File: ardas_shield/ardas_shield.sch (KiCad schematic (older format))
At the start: 36 parts, among them CON1 SD_Card, IC1 DS1307, P1 CONN_10, P10 CONN_01X03, P2 CONN_8, P3 CONN_8, P4 CONN_ICSP, P5 CONN_6, P6 TTL_COMM, P7 CONN_01X03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

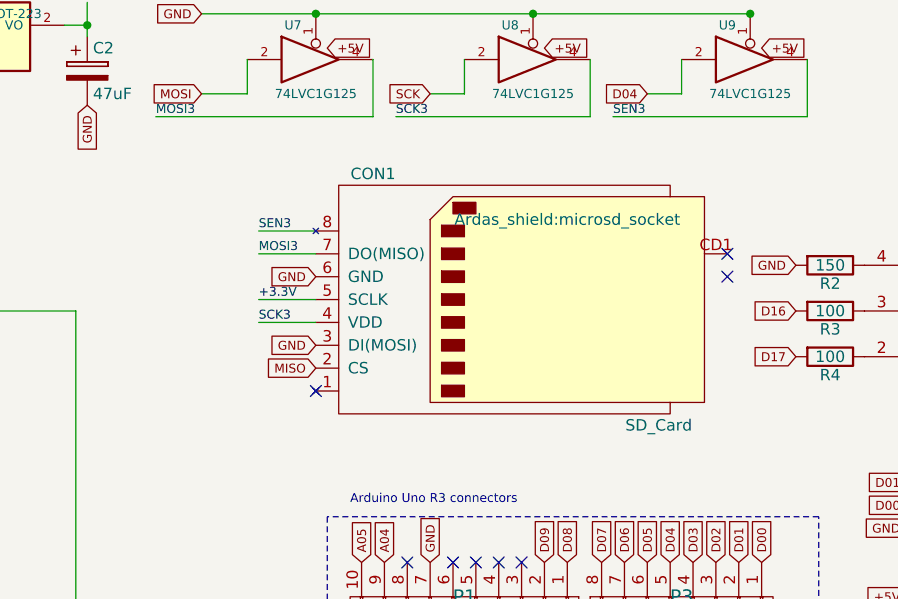
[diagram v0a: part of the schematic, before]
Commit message: changed resitances arrays footprints
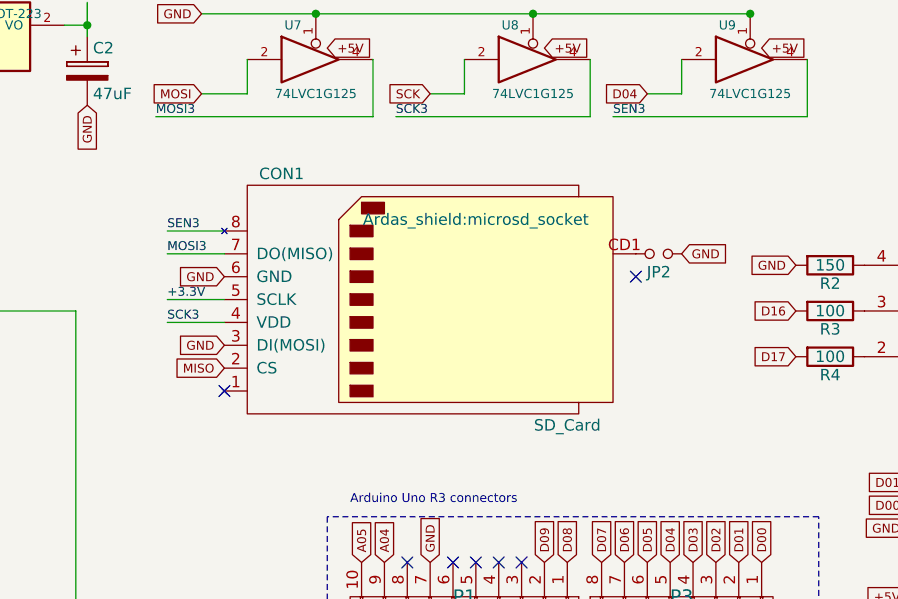
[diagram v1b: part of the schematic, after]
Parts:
- added JP2: Jumper_NO_Small, RTC_Ardas_test:small_no_jumper, symbol Jumper_NO_Small
- RP1, RP2, RP3, RP4, RP5: footprint Ardas_shield:R_Array_Convex_4x1206 -> kicad-gfa local:R_Array_Convex_4x0603
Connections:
- net GND: now also JP2.1
- net at CON1.CD1: now also JP2.2
- no-connect marks 22 -> 21
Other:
- moved on the sheet: CON1
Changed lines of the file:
@@
 $EndDescr
 $Comp
-L PWR_FLAG #FLG01
+L PWR_FLAG #FLG2
 U 1 1 55782956
 P 800 1100
-F 0 "#FLG01" H 800 1195 30  0001 C CNN
+F 0 "#FLG2" H 800 1195 30  0001 C CNN
 F 1 "PWR_FLAG" H 800 1280 30  0000 C CNN
 F 2 "" H 800 1100 60  0000 C CNN
@@
 NoConn ~ 4300 6600
 $Comp
-L +5V #PWR02
+L +5V #PWR1
 U 1 1 56548203
 P 1000 700
-F 0 "#PWR02" H 1000 790 20  0001 C CNN
+F 0 "#PWR1" H 1000 790 20  0001 C CNN
 F 1 "+5V" H 1000 790 30  0000 C CNN
 F 2 "" H 1000 700 60  0000 C CNN
@@
 D14
 $Comp
-L PWR_FLAG #FLG03
+L PWR_FLAG #FLG1
 U 1 1 55782922
 P 800 700
-F 0 "#FLG03" H 800 795 30  0001 C CNN
+F 0 "#FLG1" H 800 795 30  0001 C CNN
 F 1 "PWR_FLAG" H 800 880 30  0000 C CNN
 F 2 "" H 800 700 60  0000 C CNN
@@
 Text GLabel 10600 1250 0    39   Input ~ 0
 SCK
-Text GLabel 10100 2350 0    39   Input ~ 0
-GND
-Text GLabel 10100 2450 0    39   Input ~ 0
+Text GLabel 9700 2350 0    39   Input ~ 0
+GND
+Text GLabel 9700 2450 0    39   Input ~ 0
 MISO
-Text GLabel 10100 2050 0    39   Input ~ 0
-GND
-Text Label 9850 2250 0    39   ~ 0
+Text GLabel 9700 2050 0    39   Input ~ 0
+GND
+Text Label 9450 2250 0    39   ~ 0
 SCK3
-Text Label 9850 2150 0    39   ~ 0
+Text Label 9450 2150 0    39   ~ 0
 +3.3V
 Text GLabel 8600 1250 3    39   Input ~ 0
 GND
-Text Label 9850 1950 0    39   ~ 0
+Text Label 9450 1950 0    39   ~ 0
 MOSI3
-Text Label 9850 1850 0    39   ~ 0
+Text Label 9450 1850 0    39   ~ 0
 SEN3
 $Comp
@@
 Text GLabel 12050 4150 2    39   Input ~ 0
 GND
-NoConn ~ 10100 2550
+NoConn ~ 9700 2550
 Text Notes 12850 3050 0    39   ~ 0
 Rx
@@
 F 0 "RP1" H 2450 2850 50  0000 C CNN
 F 1 "R_4x4.7k" H 2450 2350 50  0000 C CNN
-F 2 "Ardas_shield:R_Array_Convex_4x1206" H 2450 2400 60  0001 C CNN
+F 2 "kicad-gfa local:R_Array_Convex_4x0603" H 2450 2400 60  0001 C CNN
 F 3 "" H 2450 2400 60  0000 C CNN
 	1    2450 2400
@@
 F 0 "RP4" H 6750 5900 50  0000 C CNN
 F 1 "R_4x10k" H 6750 5400 50  0000 C CNN
-F 2 "Ardas_shield:R_Array_Convex_4x1206" H 6750 5450 60  0001 C CNN
+F 2 "kicad-gfa local:R_Array_Convex_4x0603" H 6750 5450 60  0001 C CNN
 F 3 "https://github.com/UMONS-GFA/kicad-gfa.pretty/blob/master/datasheets/1730408.pdf" H 6750 5450 60  0001 C CNN
 	1    6750 5450
@@
 F 0 "RP3" H 6750 4400 50  0000 C CNN
 F 1 "R_4x10k" H 6750 3900 50  0000 C CNN
-F 2 "Ardas_shield:R_Array_Convex_4x1206" H 6750 3950 60  0001 C CNN
+F 2 "kicad-gfa local:R_Array_Convex_4x0603" H 6750 3950 60  0001 C CNN
 F 3 "https://github.com/UMONS-GFA/kicad-gfa.pretty/blob/master/datasheets/1730408.pdf" H 6750 3950 60  0001 C CNN
 	1    6750 3950
@@
 NoConn ~ 11550 4150
 $Comp
-L GND #PWR04
+L GND #PWR2
 U 1 1 56583A97
 P 1000 1200
-F 0 "#PWR04" H 1000 1200 30  0001 C CNN
+F 0 "#PWR2" H 1000 1200 30  0001 C CNN
 F 1 "GND" H 1000 1130 30  0001 C CNN
 F 2 "" H 1000 1200 60  0000 C CNN
@@
 F 0 "RP2" H 4450 3550 50  0000 C CNN
 F 1 "R_4x10k" H 4450 3050 50  0000 C CNN
-F 2 "Ardas_shield:R_Array_Convex_4x1206" H 4450 3100 60  0001 C CNN
+F 2 "kicad-gfa local:R_Array_Convex_4x0603" H 4450 3100 60  0001 C CNN
 F 3 "" H 4450 3100 60  0000 C CNN
 	1    4450 3100
@@
 F 0 "RP5" H 7450 3550 50  0000 C CNN
 F 1 "R_4x10k" H 7450 3050 50  0000 C CNN
-F 2 "Ardas_shield:R_Array_Convex_4x1206" H 7450 3100 60  0001 C CNN
+F 2 "kicad-gfa local:R_Array_Convex_4x0603" H 7450 3100 60  0001 C CNN
 F 3 "https://github.com/UMONS-GFA/kicad-gfa.pretty/blob/master/datasheets/1730408.pdf" H 7450 3100 60  0001 C CNN
 	1    7450 3100
@@
 NoConn ~ 4600 2100
 NoConn ~ 2000 4200
-NoConn ~ 11900 1950
-NoConn ~ 11900 2050
+NoConn ~ 11500 2050
 NoConn ~ 13200 1000
 $Comp
 L SD_Card CON1
 U 1 1 5655FE06
-P 11000 2150
-F 0 "CON1" H 10350 2700 50  0000 C CNN
-F 1 "SD_Card" H 11600 1600 50  0000 C CNN
-F 2 "Ardas_shield:microsd_socket" H 11200 2500 50  0000 C CNN
-F 3 "" H 11000 2150 60  0000 C CNN
-	1    11000 2150
+P 10600 2150
+F 0 "CON1" H 9950 2700 50  0000 C CNN
+F 1 "SD_Card" H 11200 1600 50  0000 C CNN
+F 2 "Ardas_shield:microsd_socket" H 10800 2500 50  0000 C CNN
+F 3 "" H 10600 2150 60  0000 C CNN
+	1    10600 2150
 	1    0    0    -1
 $EndComp
@@
 	12300 5000 12300 3100
 Wire Wire Line
-	10100 1850 9850 1850
-Wire Wire Line
-	10100 1950 9850 1950
-Wire Wire Line
-	10100 2150 9850 2150
-Wire Wire Line
-	10100 2250 9850 2250
+	9700 1850 9450 1850
+Wire Wire Line
+	9700 1950 9450 1950
+Wire Wire Line
+	9700 2150 9450 2150
+Wire Wire Line
+	9700 2250 9450 2250
 Wire Wire Line
 	11700 1250 11550 1250
@@
 NoConn ~ 11950 4800
 NoConn ~ 12050 4800
+$Comp
+L Jumper_NO_Small JP2
+U 1 1 569E9D5A
+P 11600 1950
+F 0 "JP2" H 11600 2030 50  0000 C CNN
+F 1 "Jumper_NO_Small" H 11610 1890 50  0001 C CNN
+F 2 "RTC_Ardas_test:small_no_jumper" H 11600 1950 50  0001 C CNN
+F 3 "" H 11600 1950 50  0000 C CNN
+	1    11600 1950
+	-1   0    0    1
+$EndComp
+Text GLabel 11700 1950 2    39   Input ~ 0
+GND
 $EndSCHEMATC

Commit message: add details for BOM
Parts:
- BT1: MFN (none) -> KEYSTONE; MFP (none) -> 3000; Order_Code (none) -> 1650692
- CON1: MFN (none) -> MOLEX; MFP (none) -> 503182-1853; Order_Code (none) -> 2334075
- IC1: MFN (none) -> MAXIM INTEGRATED PRODUCTS; MFP (none) -> DS1307ZN+; Order_Code (none) -> 9725253
- P1: Contact_Termination_Type (none) -> Through Hole; MFN (none) -> FCI; MFP (none) -> 69190-410HLF; Order_Code (none) -> 1278412; Pitch_Spacing (none) -> 2.54mm
- P3: Contact_Termination _Type (none) -> Through Hole; MFN (none) -> FCI; MFP (none) -> 68000-208HLF; Order_Code (none) -> 1924194; Pitch_Spacing (none) -> 2.54mm
- P4: Contact_Termination_Type (none) -> Through Hole; Gender (none) -> Receptacle; MFN (none) -> TE CONNECTIVITY / AMP; MFP (none) -> 5-534206-3; Order_Code (none) -> 1266033; Pitch_Spacing (none) -> 2.54mm
- P5:  Pitch_Spacing (none) -> 2.54mm; Contact_Termination_Type (none) -> Through Hole; MFN (none) -> MOLEX; MFP (none) -> 22-28-4064; Order_Code (none) -> 2132359
- P6: Contact_Termination_Type (none) -> Through Hole; Gender (none) -> Header; MFN (none) -> MULTICOMP; MFP (none) -> MC34747; Order_Code (none) -> 1593427; Pitch_Spacing (none) -> 2.54mm
- R2: Case_Style (none) -> 0805 [2012 Metric]; MFN (none) -> YAGEO (PHYCOMP); MFP (none) -> RC0805JR-07150RL; Order_Code (none) -> 9233903RL
- R3: Case_Style (none) -> 0805 [2012 Metric]; MFN (none) -> YAGEO (PHYCOMP); MFP (none) -> RC0805JR-07100RL; Order_Code (none) -> 9233881
- R4: Case_Style (none) -> 805 [2012 Metric]; MFN (none) -> YAGEO (PHYCOMP); MFP (none) -> RC0805JR-07100RL; Order_Code (none) -> 9233881
- U1: MFN (none) -> TEXAS INSTRUMENTS; MFP (none) -> SN74HC595DW; Order_Code (none) -> 1595418
- U2, U4: MFN (none) -> TEXAS INSTRUMENTS; MFP (none) -> SN74HC165D; Order_Code (none) -> 9591192
- U3, U6: MFN (none) -> TEXAS INSTRUMENTS; MFP (none) -> SN74LV8154PW; Order_Code (none) -> 1741273
- U5: MFN (none) -> STMICROELECTRONICS; MFP (none) -> LD1117S33TR; Order_Code (none) -> 1202826
- X1: MFN (none) -> ABRACON; MFP (none) -> ABS07-32.768KHZ-1-T; Order_Code (none) -> 2467865
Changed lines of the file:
@@
 $EndDescr
 $Comp
-L PWR_FLAG #FLG2
+L PWR_FLAG #FLG01
 U 1 1 55782956
 P 800 1100
-F 0 "#FLG2" H 800 1195 30  0001 C CNN
+F 0 "#FLG01" H 800 1195 30  0001 C CNN
 F 1 "PWR_FLAG" H 800 1280 30  0000 C CNN
 F 2 "" H 800 1100 60  0000 C CNN
@@
 F 2 "Ardas_shield:SOIC-8-N" H 1800 3250 50  0001 C CNN
 F 3 "https://github.com/UMONS-GFA/kicad-gfa.pretty/blob/master/datasheets/46359.pdf" H 1800 3100 60  0001 C CNN
+F 4 "9725253" H 1800 3100 60  0001 C CNN "Order_Code"
+F 5 "MAXIM INTEGRATED PRODUCTS" H 1800 3100 60  0001 C CNN "MFN"
+F 6 "DS1307ZN+" H 1800 3100 60  0001 C CNN "MFP"
 	1    1800 3100
 	0    1    -1   0
@@
 F 1 "CRYSTAL" H 1800 4100 60  0000 C CNN
 F 2 "Ardas_shield:XTAL_ABRACON_ABS07" H 1800 4250 60  0001 C CNN
-F 3 "~" H 1800 4250 60  0000 C CNN
+F 3 "https://github.com/UMONS-GFA/kicad-gfa.pretty/blob/master/datasheets/1883680.pdf" H 1800 4250 60  0001 C CNN
+F 4 "2467865" H 1800 4250 60  0001 C CNN "Order_Code"
+F 5 "ABRACON" H 1800 4250 60  0001 C CNN "MFN"
+F 6 "ABS07-32.768KHZ-1-T" H 1800 4250 60  0001 C CNN "MFP"
 	1    1800 4250
 	-1   0    0    -1
@@
 F 2 "Ardas_shield:TSSOP-20_4.4x6.5mm_Pitch0.65mm" H 5200 4150 60  0001 C CNN
 F 3 "https://github.com/UMONS-GFA/kicad-gfa.pretty/blob/master/datasheets/1996491.pdf" H 5200 4150 60  0001 C CNN
+F 4 " 1741273" H 5200 4150 60  0001 C CNN "Order_Code"
+F 5 "TEXAS INSTRUMENTS" H 5200 4150 60  0001 C CNN "MFN"
+F 6 "SN74LV8154PW" H 5200 4150 60  0001 C CNN "MFP"
 	1    5200 4150
 	0    1    1    0
@@
 F 2 "Ardas_shield:SOIC-16_3.9x9.9mm_Pitch1.27mm" H 4900 6350 60  0001 C CNN
 F 3 "https://github.com/UMONS-GFA/kicad-gfa.pretty/blob/master/datasheets/1831348.pdf" H 4900 6350 60  0001 C CNN
+F 4 "9591192" H 4900 6350 60  0001 C CNN "Order_Code"
+F 5 "TEXAS INSTRUMENTS" H 4900 6350 60  0001 C CNN "MFN"
+F 6 "SN74HC165D" H 4900 6350 60  0001 C CNN "MFP"
 	1    4900 6350
 	1    0    0    -1
@@
 F 2 "Ardas_shield:TSSOP-20_4.4x6.5mm_Pitch0.65mm" H 8600 4150 60  0001 C CNN
 F 3 "https://github.com/UMONS-GFA/kicad-gfa.pretty/blob/master/datasheets/1996491.pdf" H 8600 4150 60  0001 C CNN
+F 4 "1741273" H 8600 4150 60  0001 C CNN "Order_Code"
+F 5 "TEXAS INSTRUMENTS" H 8600 4150 60  0001 C CNN "MFN"
+F 6 "SN74LV8154PW" H 8600 4150 60  0001 C CNN "MFP"
 	1    8600 4150
 	0    1    1    0
@@
 F 2 "Ardas_shield:SOIC-16_3.9x9.9mm_Pitch1.27mm" H 8300 6350 60  0001 C CNN
 F 3 "https://github.com/UMONS-GFA/kicad-gfa.pretty/blob/master/datasheets/1831348.pdf" H 8300 6350 60  0001 C CNN
+F 4 "9591192" H 8300 6350 60  0001 C CNN "Order_Code"
+F 5 "TEXAS INSTRUMENTS" H 8300 6350 60  0001 C CNN "MFN"
+F 6 "SN74HC165D" H 8300 6350 60  0001 C CNN "MFP"
 	1    8300 6350
 	1    0    0    -1
@@
 F 2 "Ardas_shield:Pin_Header_Straight_1x10" H 10750 3500 60  0001 C CNN
 F 3 "" H 10750 3500 60  0000 C CNN
+F 4 "1278412" V 10750 3500 60  0001 C CNN "Order_Code"
+F 5 "FCI" V 10750 3500 60  0001 C CNN "MFN"
+F 6 "69190-410HLF" V 10750 3500 60  0001 C CNN "MFP"
+F 7 "2.54mm" V 10750 3500 60  0001 C CNN "Pitch_Spacing"
+F 8 "Through Hole" V 10750 3500 60  0001 C CNN "Contact_Termination_Type"
 	1    10750 3500
 	0    1    1    0
@@
 F 2 "Ardas_shield:Pin_Header_Straight_1x08" H 11700 3500 60  0001 C CNN
 F 3 "" H 11700 3500 60  0000 C CNN
+F 4 "1924194" V 11700 3500 60  0001 C CNN "Order_Code"
+F 5 "FCI" V 11700 3500 60  0001 C CNN "MFN"
+F 6 "68000-208HLF" V 11700 3500 60  0001 C CNN "MFP"
+F 7 "2.54mm" V 11700 3500 60  0001 C CNN "Pitch_Spacing"
+F 8 "Through Hole " V 11700 3500 60  0001 C CNN "Contact_Termination _Type"
 	1    11700 3500
 	0    1    1    0
@@
 F 2 "Ardas_shield:Pin_Header_Straight_1x06" H 11800 4600 60  0001 C CNN
 F 3 "" H 11800 4600 60  0000 C CNN
+F 4 "2132359" V 11800 4600 60  0001 C CNN "Order_Code"
+F 5 "MOLEX" V 11800 4600 60  0001 C CNN "MFN"
+F 6 "22-28-4064" V 11800 4600 60  0001 C CNN "MFP"
+F 7 "2.54mm" V 11800 4600 60  0001 C CNN " Pitch_Spacing"
+F 8 "Through Hole" V 11800 4600 60  0001 C CNN "Contact_Termination_Type"
 	1    11800 4600
 	0    -1   -1   0
@@
 NoConn ~ 4300 6600
 $Comp
-L +5V #PWR1
+L +5V #PWR02
 U 1 1 56548203
 P 1000 700
-F 0 "#PWR1" H 1000 790 20  0001 C CNN
+F 0 "#PWR02" H 1000 790 20  0001 C CNN
 F 1 "+5V" H 1000 790 30  0000 C CNN
 F 2 "" H 1000 700 60  0000 C CNN
@@
 F 2 "Ardas_shield:Pin_Header_Angled_1x03" H 12900 3050 60  0001 C CNN
 F 3 "" H 12900 3050 60  0000 C CNN
+F 4 "1593427" H 12900 3050 60  0001 C CNN "Order_Code"
+F 5 "MULTICOMP" H 12900 3050 60  0001 C CNN "MFN"
+F 6 "MC34747" H 12900 3050 60  0001 C CNN "MFP"
+F 7 "2.54mm" H 12900 3050 60  0001 C CNN "Pitch_Spacing"
+F 8 "Through Hole " H 12900 3050 60  0001 C CNN "Contact_Termination_Type"
+F 9 "Header" H 12900 3050 60  0001 C CNN "Gender"
 	1    12900 3050
 	1    0    0    -1
@@
 D14
 $Comp
-L PWR_FLAG #FLG1
+L PWR_FLAG #FLG03
 U 1 1 55782922
 P 800 700
-F 0 "#FLG1" H 800 795 30  0001 C CNN
+F 0 "#FLG03" H 800 795 30  0001 C CNN
 F 1 "PWR_FLAG" H 800 880 30  0000 C CNN
 F 2 "" H 800 700 60  0000 C CNN
@@
 F 1 "LD1117S33TR" H 8600 1200 40  0000 C CNN
 F 2 "Ardas_shield:SOT-223" H 8600 1100 40  0000 C CNN
-F 3 "" H 8600 1000 60  0000 C CNN
+F 3 "https://github.com/UMONS-GFA/kicad-gfa.pretty/blob/master/datasheets/1776449.pdf" H 8600 1000 60  0001 C CNN
+F 4 "1202826" H 8600 1000 60  0001 C CNN "Order_Code"
+F 5 "STMICROELECTRONICS" H 8600 1000 60  0001 C CNN "MFN"
+F 6 " LD1117S33TR" H 8600 1000 60  0001 C CNN "MFP"
 	1    8600 1000
 	1    0    0    -1
@@
 F 2 "Ardas_shield:Socket_Strip_Straight_2x03" H 11800 2850 60  0001 C CNN
 F 3 "" H 11800 2850 60  0000 C CNN
+F 4 "1266033" H 11800 4050 60  0001 C CNN "Order_Code"
+F 5 "TE CONNECTIVITY / AMP " H 11800 4050 60  0001 C CNN "MFN"
+F 6 "5-534206-3" H 11800 4050 60  0001 C CNN "MFP"
+F 7 "2.54mm" H 11800 4050 60  0001 C CNN "Pitch_Spacing"
+F 8 "Through Hole" H 11800 4050 60  0001 C CNN "Contact_Termination_Type"
+F 9 "Receptacle" H 11800 4050 60  0001 C CNN "Gender"
 	1    11800 4050
 	1    0    0    -1
@@
 NoConn ~ 11550 4150
 $Comp
-L GND #PWR2
+L GND #PWR04
 U 1 1 56583A97
 P 1000 1200
-F 0 "#PWR2" H 1000 1200 30  0001 C CNN
+F 0 "#PWR04" H 1000 1200 30  0001 C CNN
 F 1 "GND" H 1000 1130 30  0001 C CNN
 F 2 "" H 1000 1200 60  0000 C CNN
@@
 F 1 "Battery" H 1000 3000 50  0000 L CNN
 F 2 "Ardas_shield:BATTERY_KEYSTONE_12mm" V 900 3090 60  0001 C CNN
-F 3 "" V 900 3090 60  0000 C CNN
+F 3 "https://github.com/UMONS-GFA/kicad-gfa.pretty/blob/master/datasheets/1696457.pdf" V 900 3090 60  0001 C CNN
+F 4 "1650692 " H 900 3050 60  0001 C CNN "Order_Code"
+F 5 "KEYSTONE " H 900 3050 60  0001 C CNN "MFN"
+F 6 "3000" H 900 3050 60  0001 C CNN "MFP"
 	1    900  3050
 	1    0    0    -1
@@
 F 2 "Ardas_shield:SOIC-16_7.5x10.3mm_Pitch1.27mm" H 3900 1650 60  0001 C CNN
 F 3 "https://github.com/UMONS-GFA/kicad-gfa.pretty/blob/master/datasheets/1970412.pdf" H 3900 1650 60  0001 C CNN
+F 4 "1595418" H 3900 1650 60  0001 C CNN "Order_Code"
+F 5 "TEXAS INSTRUMENTS " H 3900 1650 60  0001 C CNN "MFN"
+F 6 "SN74HC595DW" H 3900 1650 60  0001 C CNN "MFP"
 	1    3900 1650
 	1    0    0    -1
@@
 F 1 "SD_Card" H 11200 1600 50  0000 C CNN
 F 2 "Ardas_shield:microsd_socket" H 10800 2500 50  0000 C CNN
-F 3 "" H 10600 2150 60  0000 C CNN
+F 3 "https://github.com/UMONS-GFA/kicad-gfa.pretty/blob/master/datasheets/1717993.pdf" H 10600 2150 60  0001 C CNN
+F 4 "2334075" H 10600 2150 60  0001 C CNN "Order_Code"
+F 5 "MOLEX" H 10600 2150 60  0001 C CNN "MFN"
+F 6 "503182-1853" H 10600 2150 60  0001 C CNN "MFP"
 	1    10600 2150
 	1    0    0    -1
@@
 F 2 "Ardas_shield:R_0805" V 12280 2000 50  0001 C CNN
 F 3 "" H 12350 2000 50  0000 C CNN
+F 4 "9233903RL " V 12350 2000 60  0001 C CNN "Order_Code"
+F 5 "YAGEO (PHYCOMP) " V 12350 2000 60  0001 C CNN "MFN"
+F 6 "RC0805JR-07150RL" V 12350 2000 60  0001 C CNN "MFP"
+F 7 "0805 [2012 Metric]" V 12350 2000 60  0001 C CNN "Case_Style"
 	1    12350 2000
 	0    1    1    0
@@
 F 2 "Ardas_shield:R_0805" V 12280 2200 50  0001 C CNN
 F 3 "" H 12350 2200 50  0000 C CNN
+F 4 "9233881" V 12350 2200 60  0001 C CNN "Order_Code"
+F 5 "YAGEO (PHYCOMP) " V 12350 2200 60  0001 C CNN "MFN"
+F 6 "RC0805JR-07100RL" V 12350 2200 60  0001 C CNN "MFP"
+F 7 "0805 [2012 Metric]" V 12350 2200 60  0001 C CNN "Case_Style"
 	1    12350 2200
 	0    1    1    0
@@
 F 2 "Ardas_shield:R_0805" V 12280 2400 50  0001 C CNN
 F 3 "" H 12350 2400 50  0000 C CNN
+F 4 "9233881" V 12350 2400 60  0001 C CNN "Order_Code"
+F 5 "YAGEO (PHYCOMP)" V 12350 2400 60  0001 C CNN "MFN"
+F 6 "RC0805JR-07100RL" V 12350 2400 60  0001 C CNN "MFP"
+F 7 "805 [2012 Metric]" V 12350 2400 60  0001 C CNN "Case_Style"
 	1    12350 2400
 	0    1    1    0

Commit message: fix
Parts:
- P3: Contact_Termination _Type Through Hole -> (none); Contact_Termination_Type (none) -> Through Hole
- P5:  Pitch_Spacing 2.54mm -> (none); Pitch_Spacing (none) -> 2.54mm
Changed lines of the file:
@@
 F 6 "68000-208HLF" V 11700 3500 60  0001 C CNN "MFP"
 F 7 "2.54mm" V 11700 3500 60  0001 C CNN "Pitch_Spacing"
-F 8 "Through Hole " V 11700 3500 60  0001 C CNN "Contact_Termination _Type"
+F 8 "Through Hole " V 11700 3500 60  0001 C CNN "Contact_Termination_Type"
 	1    11700 3500
 	0    1    1    0
@@
 F 5 "MOLEX" V 11800 4600 60  0001 C CNN "MFN"
 F 6 "22-28-4064" V 11800 4600 60  0001 C CNN "MFP"
-F 7 "2.54mm" V 11800 4600 60  0001 C CNN " Pitch_Spacing"
+F 7 "2.54mm" V 11800 4600 60  0001 C CNN "Pitch_Spacing"
 F 8 "Through Hole" V 11800 4600 60  0001 C CNN "Contact_Termination_Type"
 	1    11800 4600

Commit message: modified RGB LED and SD-Card pinout and buffer VCC
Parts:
- R2: value 150 -> 4.7k
- R3: value 100 -> 10k
- R4: value 100 -> 4.7k
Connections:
- net +5V: no longer U1.16 (VCC), U7.5 (VCC), U8.5 (VCC), U9.5 (VCC)
- net GND: no longer CON1.3 (DI(MOSI))
- net MISO: now also CON1.7 (DO(MISO)); no longer CON1.2 (CS)
- net MOSI3: now also CON1.3 (DI(MOSI)); no longer CON1.7 (DO(MISO))
- net SCK3: now also CON1.5 (SCLK); no longer CON1.4 (VDD)
- net SEN3: now also CON1.2 (CS); no longer CON1.8
- net +3.3V renamed VCC
- net VCC: now also CON1.4 (VDD), U1.16 (VCC), U7.5 (VCC), U8.5 (VCC), U9.5 (VCC); no longer CON1.5 (SCLK)
- no-connect marks 21 -> 20
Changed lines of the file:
@@
 	1    0    0    -1
 $EndComp
-Text Label 9100 850  0    39   ~ 0
-+3.3V
 Text GLabel 8000 950  0    39   Input ~ 0
 +5V
@@
 Text GLabel 10600 1250 0    39   Input ~ 0
 SCK
-Text GLabel 9700 2350 0    39   Input ~ 0
-GND
-Text GLabel 9700 2450 0    39   Input ~ 0
+Text GLabel 9700 1950 0    39   Input ~ 0
 MISO
 Text GLabel 9700 2050 0    39   Input ~ 0
 GND
+Text Label 9450 2150 0    39   ~ 0
+SCK3
 Text Label 9450 2250 0    39   ~ 0
-SCK3
-Text Label 9450 2150 0    39   ~ 0
 +3.3V
 Text GLabel 8600 1250 3    39   Input ~ 0
 GND
-Text Label 9450 1950 0    39   ~ 0
+Text Label 9450 2350 0    39   ~ 0
 MOSI3
-Text Label 9450 1850 0    39   ~ 0
+Text Label 9450 2450 0    39   ~ 0
 SEN3
 $Comp
@@
 	1    0    0    -1
 $EndComp
-Text GLabel 10150 1050 2    39   Input ~ 0
-+5V
 Text GLabel 11100 1050 2    39   Input ~ 0
-+5V
++3.3V
 Text GLabel 12050 1050 2    39   Input ~ 0
-+5V
++3.3V
 $Comp
 L Battery BT1
@@
 NoConn ~ 4600 2100
 NoConn ~ 2000 4200
-NoConn ~ 11500 2050
 NoConn ~ 13200 1000
 $Comp
@@
 	12300 5000 12300 3100
 Wire Wire Line
-	9700 1850 9450 1850
-Wire Wire Line
-	9700 1950 9450 1950
-Wire Wire Line
 	9700 2150 9450 2150
 Wire Wire Line
@@
 P 12350 2000
 F 0 "R2" V 12430 2000 50  0000 C CNN
-F 1 "150" V 12350 2000 50  0000 C CNN
+F 1 "4.7k" V 12350 2000 50  0000 C CNN
 F 2 "Ardas_shield:R_0805" V 12280 2000 50  0001 C CNN
 F 3 "" H 12350 2000 50  0000 C CNN
@@
 P 12350 2200
 F 0 "R3" V 12430 2200 50  0000 C CNN
-F 1 "100" V 12350 2200 50  0000 C CNN
+F 1 "10k" V 12350 2200 50  0000 C CNN
 F 2 "Ardas_shield:R_0805" V 12280 2200 50  0001 C CNN
 F 3 "" H 12350 2200 50  0000 C CNN
@@
 P 12350 2400
 F 0 "R4" V 12430 2400 50  0000 C CNN
-F 1 "100" V 12350 2400 50  0000 C CNN
+F 1 "4.7k" V 12350 2400 50  0000 C CNN
 F 2 "Ardas_shield:R_0805" V 12280 2400 50  0001 C CNN
 F 3 "" H 12350 2400 50  0000 C CNN
@@
 Text GLabel 11700 1950 2    39   Input ~ 0
 GND
+Wire Wire Line
+	9700 2350 9450 2350
+Wire Wire Line
+	9700 2450 9450 2450
+Text GLabel 10150 1050 2    39   Input ~ 0
++3.3V
+Text GLabel 9100 850  1    39   Input ~ 0
++3.3V
 $EndSCHEMATC
